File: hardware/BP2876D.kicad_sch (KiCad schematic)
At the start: 9 parts, among them U301 BP2876

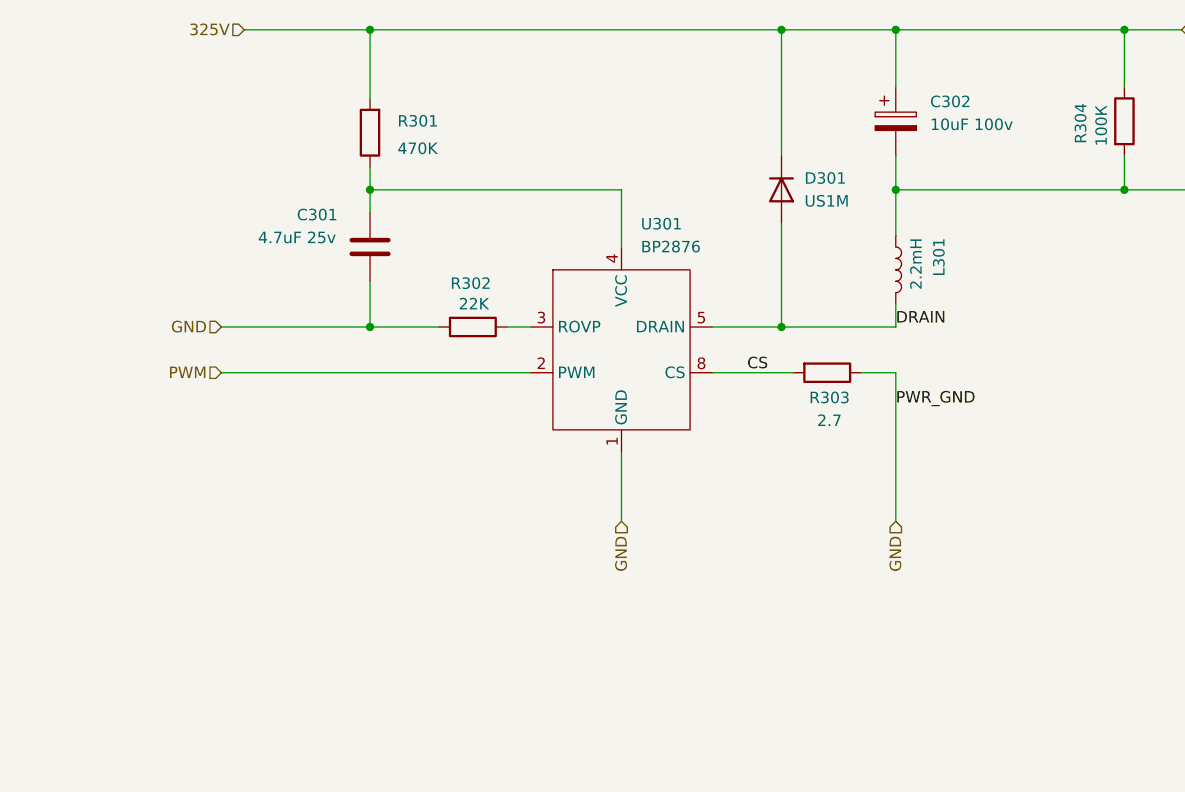
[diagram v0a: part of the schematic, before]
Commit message: Tracing 0.2
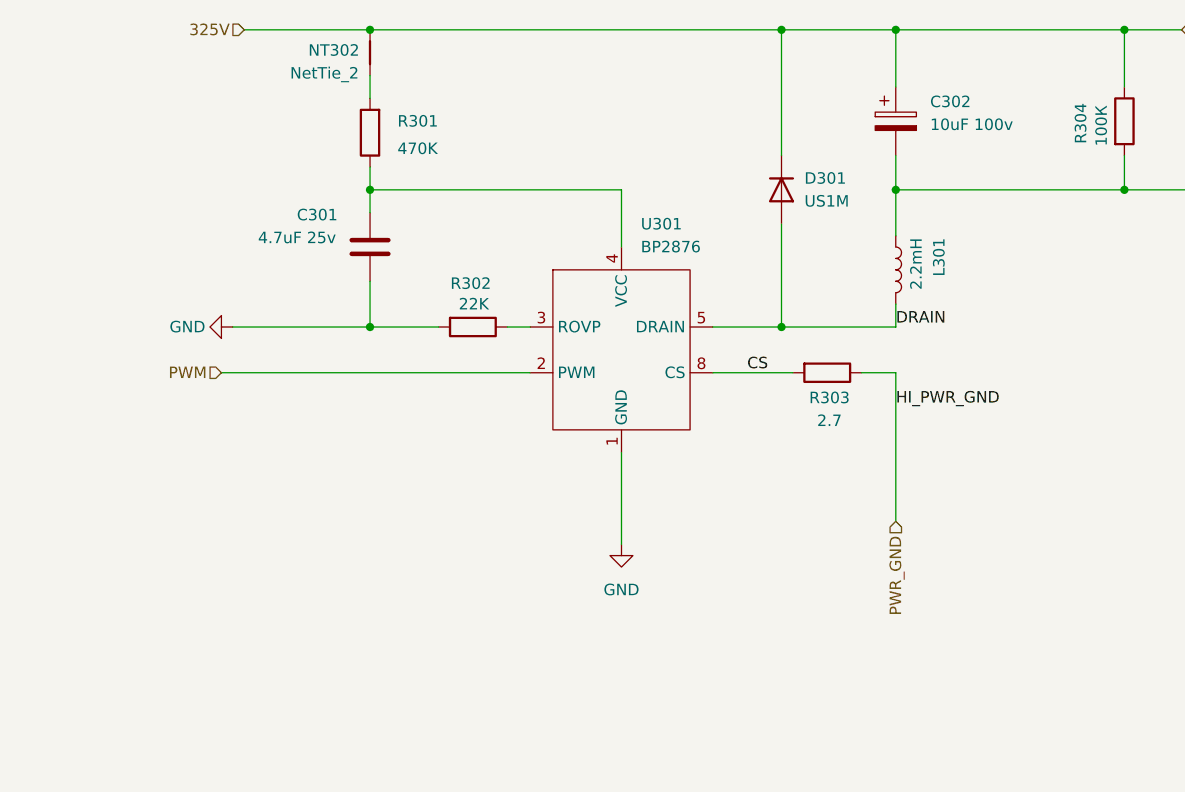
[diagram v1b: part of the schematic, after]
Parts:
- added NT302: NetTie_2, NetTie:NetTie-2_SMD_Pad0.5mm, symbol Device:NetTie_2
- L301: footprint Inductor_THT:L_Radial_D12.0mm_P5.00mm_Neosid_SD12k_style2 -> Inductor_THT:L_Radial_D9.5mm_P5.00mm_Fastron_07HVP
- R302: footprint Resistor_SMD:R_0201_0603Metric_Pad0.64x0.40mm_HandSolder -> Resistor_SMD:R_0603_1608Metric_Pad0.98x0.95mm_HandSolder
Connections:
- net 325V: now also NT302.2; no longer R301.2
- net GND: no longer R303.1
- new net: NT302.1, R301.2
- new net PWR_GND: R303.1

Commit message: Fixes
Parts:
- renumbered C302 to C301, C301 to C302, NT302 to NT301, R304 to R301, R301 to R302, R302 to R303, R303 to R304

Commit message: Use non-hand soldering footprints
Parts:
- C302: footprint Capacitor_SMD:C_0805_2012Metric_Pad1.18x1.45mm_HandSolder -> Capacitor_SMD:C_0805_2012Metric
- R301: footprint Resistor_SMD:R_1206_3216Metric_Pad1.30x1.75mm_HandSolder -> Resistor_SMD:R_1206_3216Metric
- R302: footprint Resistor_SMD:R_2512_6332Metric_Pad1.40x3.35mm_HandSolder -> Resistor_SMD:R_2512_6332Metric
- R303: footprint Resistor_SMD:R_0603_1608Metric_Pad0.98x0.95mm_HandSolder -> Resistor_SMD:R_0603_1608Metric
- R304: footprint Resistor_SMD:R_0805_2012Metric_Pad1.20x1.40mm_HandSolder -> Resistor_SMD:R_0805_2012Metric
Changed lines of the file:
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@@
 			)
 		)
-		(property "Footprint" "Resistor_SMD:R_0603_1608Metric_Pad0.98x0.95mm_HandSolder"
+		(property "Footprint" "Resistor_SMD:R_0603_1608Metric"
 			(at 166.37 83.312 90)
 			(effects
@@
 			)
 		)
-		(property "Footprint" "Capacitor_SMD:C_0805_2012Metric_Pad1.18x1.45mm_HandSolder"
+		(property "Footprint" "Capacitor_SMD:C_0805_2012Metric"
 			(at 155.9052 80.01 0)
 			(effects
@@
 			)
 		)
-		(property "Footprint" "Resistor_SMD:R_2512_6332Metric_Pad1.40x3.35mm_HandSolder"
+		(property "Footprint" "Resistor_SMD:R_2512_6332Metric"
 			(at 156.718 63.5 90)
 			(effects
@@
 			)
 		)
-		(property "Footprint" "Resistor_SMD:R_1206_3216Metric_Pad1.30x1.75mm_HandSolder"
+		(property "Footprint" "Resistor_SMD:R_1206_3216Metric"
 			(at 236.982 62.23 90)
 			(effects
@@
 			)
 		)
-		(property "Footprint" "Resistor_SMD:R_0805_2012Metric_Pad1.20x1.40mm_HandSolder"
+		(property "Footprint" "Resistor_SMD:R_0805_2012Metric"
 			(at 205.74 88.392 90)
 			(effects

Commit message: v1.1
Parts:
- R304: value 2.7 -> 2R7
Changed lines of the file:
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@@
 			)
 		)
-		(property "Value" "2.7"
+		(property "Value" "2R7"
 			(at 205.994 95.504 90)
 			(effects
